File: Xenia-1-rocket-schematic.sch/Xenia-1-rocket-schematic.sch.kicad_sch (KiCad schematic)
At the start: 10 parts

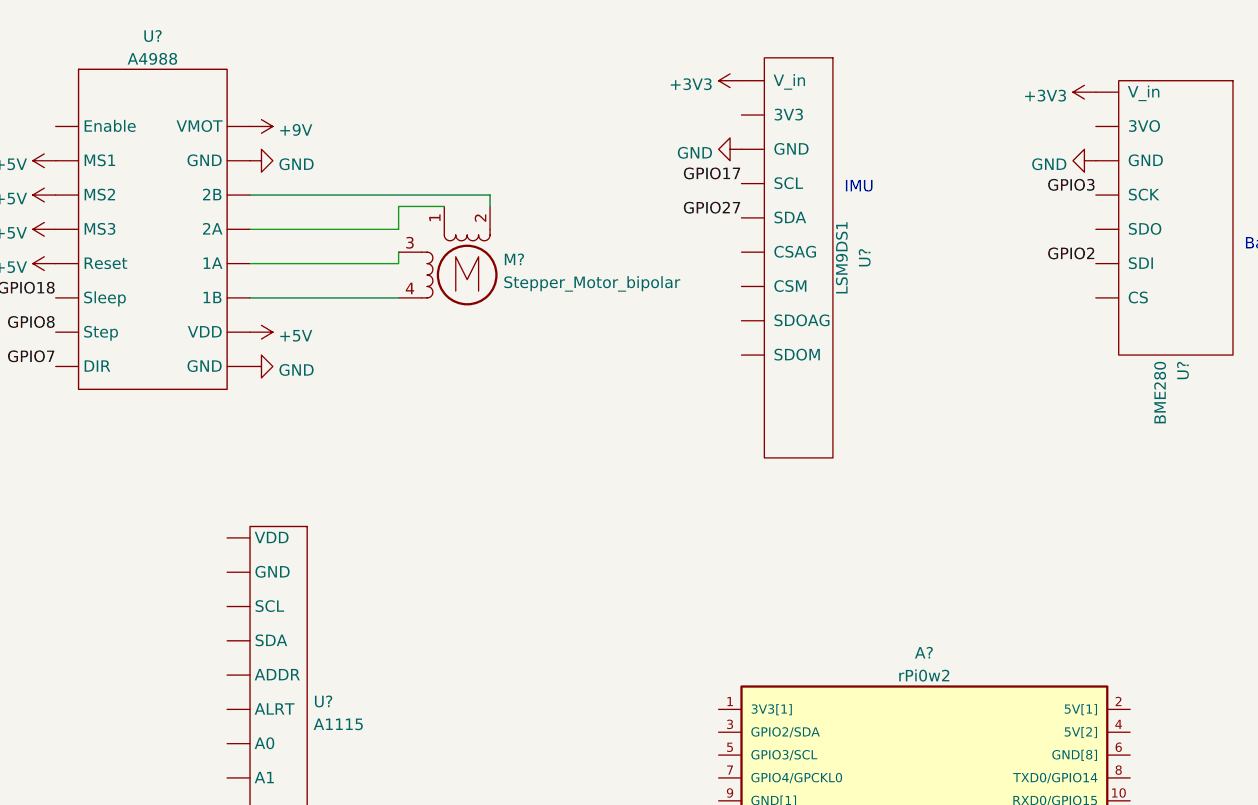
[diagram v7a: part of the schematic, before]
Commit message: Schematic updates
Changed GPIO pins so SCL and SDA are assigned. Also put pins on the Analog to Digital converter.
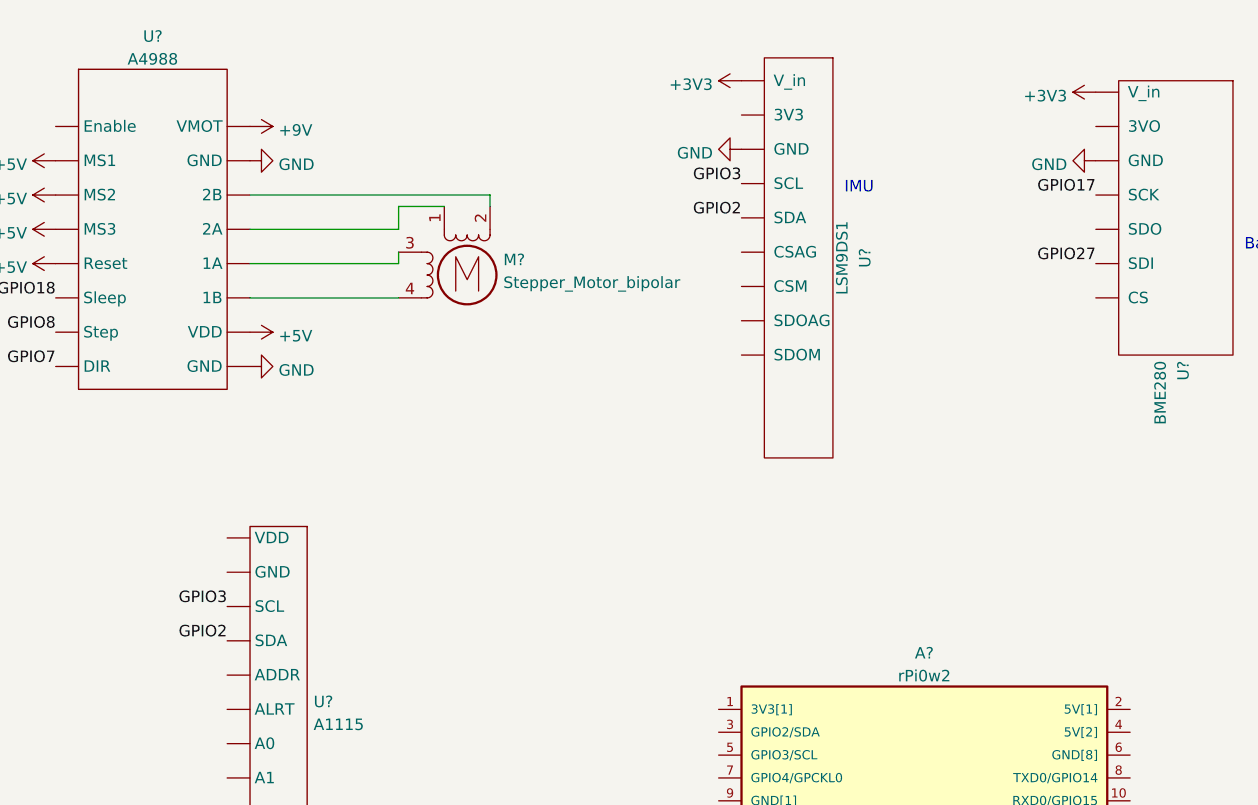
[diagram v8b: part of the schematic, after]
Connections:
- net GPIO17: now also U?.~ (V_in); no longer U?.~ (V_in)
- net GPIO2: now also U?. (VDD), U?.~ (V_in); no longer U?.~ (V_in)
- net GPIO27: now also U?.~ (V_in); no longer U?.~ (V_in)
- net GPIO3: now also U?. (VDD), U?.~ (V_in); no longer U?.~ (V_in)
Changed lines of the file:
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@@
     (effects (font (size 1.27 1.27)) (justify right bottom))
   )
-  (label "GPIO2" (at 137.16 41.91 180)
+  (label "GPIO2" (at 97.79 36.83 180)
+    (effects (font (size 1.27 1.27)) (justify right bottom))
+  )
+  (label "GPIO3" (at 40.64 80.01 180)
     (effects (font (size 1.27 1.27)) (justify right bottom))
   )
   (label "GPIO22" (at 251.46 16.51 180)
+    (effects (font (size 1.27 1.27)) (justify right bottom))
+  )
+  (label "GPIO27" (at 137.16 41.91 180)
     (effects (font (size 1.27 1.27)) (justify right bottom))
   )
@@
   )
   (label "GPIO10" (at 251.46 20.32 180)
+    (effects (font (size 1.27 1.27)) (justify right bottom))
+  )
+  (label "GPIO2" (at 40.64 83.82 180)
     (effects (font (size 1.27 1.27)) (justify right bottom))
   )
@@
     (effects (font (size 1.27 1.27)) (justify right bottom))
   )
+  (label "GPIO17" (at 137.16 34.29 180)
+    (effects (font (size 1.27 1.27)) (justify right bottom))
+  )
   (label "GPIO6" (at 251.46 35.56 180)
     (effects (font (size 1.27 1.27)) (justify right bottom))
@@
   )
   (label "GPIO26" (at 251.46 46.99 180)
+    (effects (font (size 1.27 1.27)) (justify right bottom))
+  )
+  (label "GPIO3" (at 97.79 33.02 180)
     (effects (font (size 1.27 1.27)) (justify right bottom))
   )
@@
     (effects (font (size 1.27 1.27)) (justify right bottom))
   )
-  (label "GPIO27" (at 97.79 36.83 180)
-    (effects (font (size 1.27 1.27)) (justify right bottom))
-  )
   (label "GPIO15" (at 251.46 54.61 180)
-    (effects (font (size 1.27 1.27)) (justify right bottom))
-  )
-  (label "GPIO17" (at 97.79 33.02 180)
     (effects (font (size 1.27 1.27)) (justify right bottom))
   )
@@
     (effects (font (size 1.27 1.27)) (justify right bottom))
   )
-  (label "GPIO3" (at 137.16 34.29 180)
-    (effects (font (size 1.27 1.27)) (justify right bottom))
-  )
